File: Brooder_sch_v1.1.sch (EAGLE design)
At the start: 28 parts, among them J1 DCJ0202, U1 328P

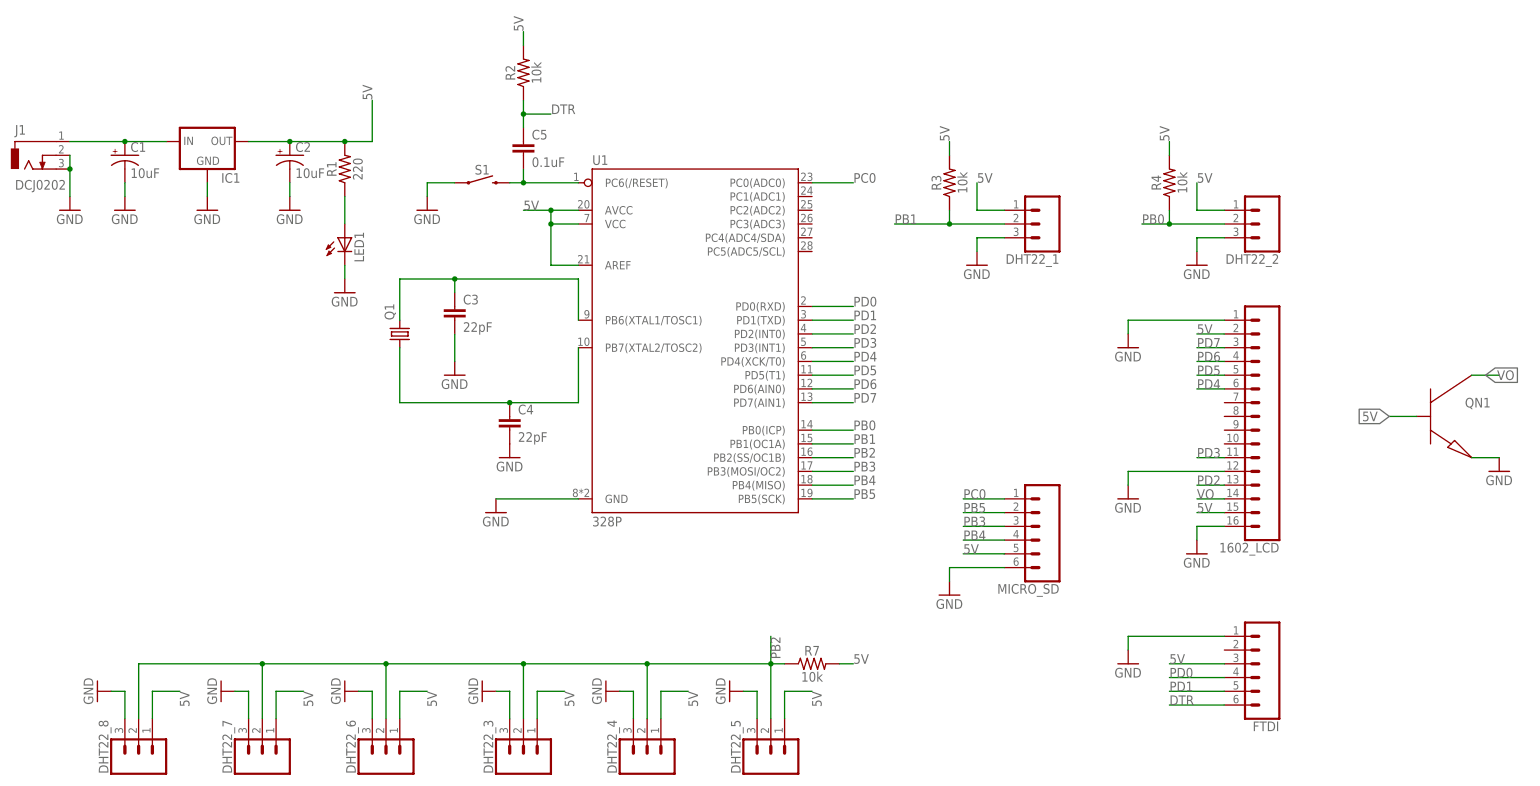
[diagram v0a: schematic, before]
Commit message: Adds the PCB layout
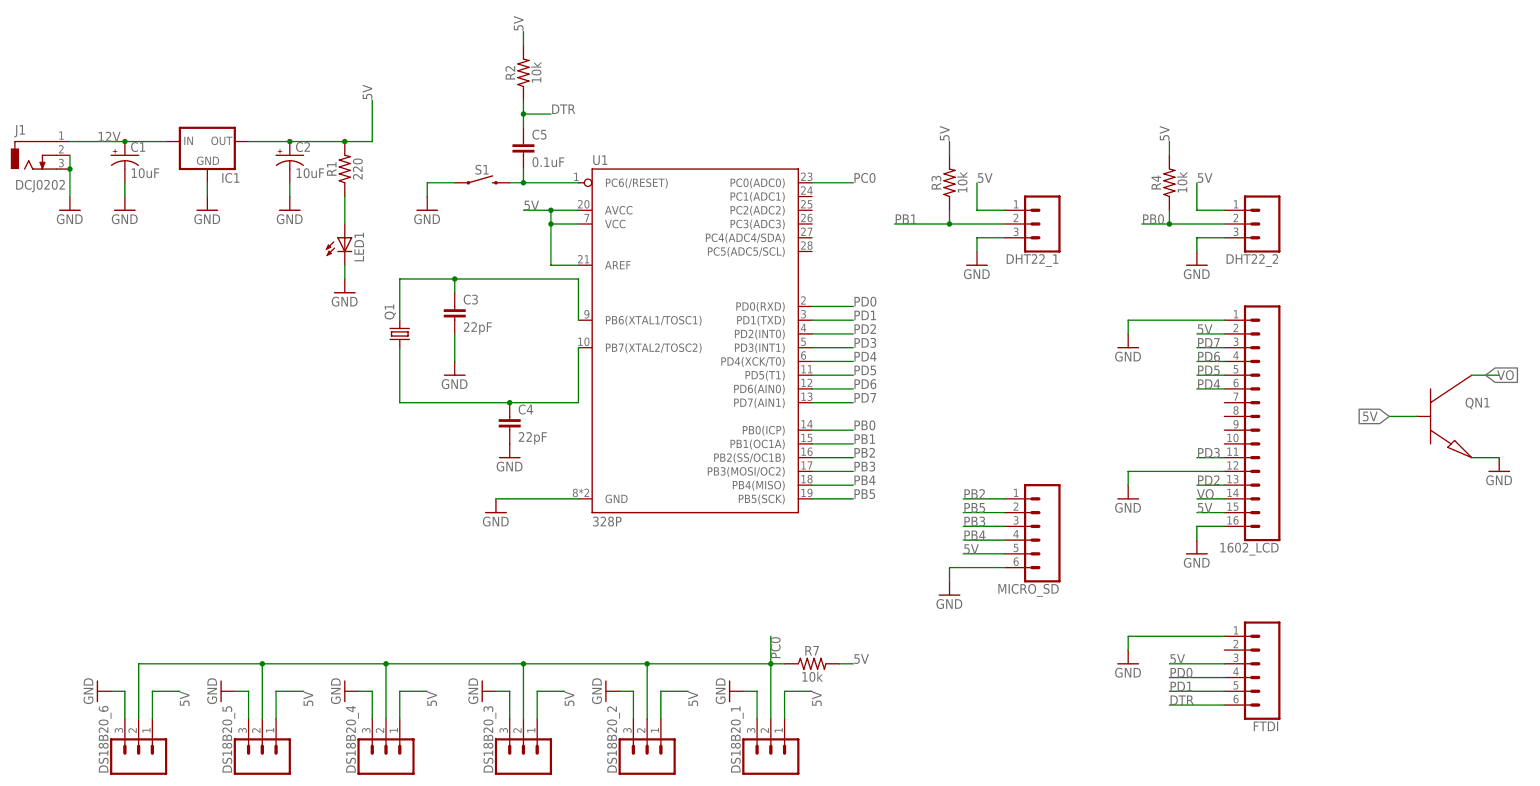
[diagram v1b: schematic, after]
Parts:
- renumbered DHT22_3 to DS18B20_3, DHT22_4 to DS18B20_2, DHT22_5 to DS18B20_1, DHT22_6 to DS18B20_4, DHT22_7 to DS18B20_5, DHT22_8 to DS18B20_6
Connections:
- net N$1 renamed 12V
- net PB2: now also MICRO_SD.1; no longer DS18B20_1.2, DS18B20_2.2, DS18B20_3.2, DS18B20_4.2, DS18B20_5.2, DS18B20_6.2, R7.1
- net PC0: now also DS18B20_1.2, DS18B20_2.2, DS18B20_3.2, DS18B20_4.2, DS18B20_5.2, DS18B20_6.2, R7.1; no longer MICRO_SD.1

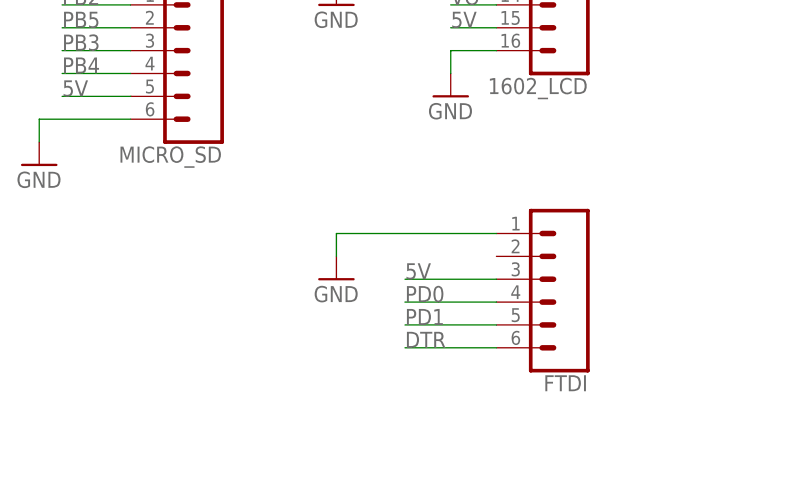
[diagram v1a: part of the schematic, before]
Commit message: Changes the lcd positioning, moves the microSD and corrects the FTDI pin mapping
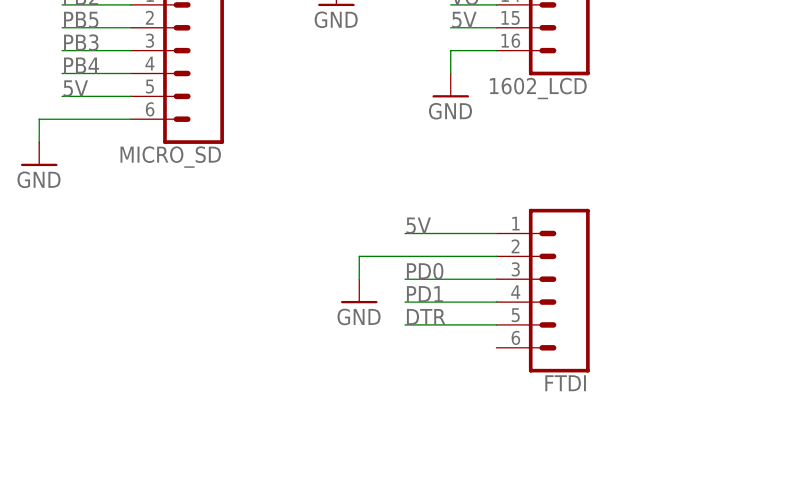
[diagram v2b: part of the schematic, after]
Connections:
- net 5V: now also FTDI.1; no longer FTDI.3
- net DTR: now also FTDI.5; no longer FTDI.6
- net GND: now also FTDI.2; no longer FTDI.1
- net PD0: now also FTDI.3; no longer FTDI.4
- net PD1: now also FTDI.4; no longer FTDI.5
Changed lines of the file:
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@@
 <part name="GND17" library="supply1" library_urn="urn:adsk.eagle:library:371" deviceset="GND" device=""/>
 <part name="FTDI" library="SparkFun-Connectors" deviceset="CONN_06" device="NO_SILK_FEMALE_PTH"/>
-<part name="GND18" library="supply1" library_urn="urn:adsk.eagle:library:371" deviceset="GND" device=""/>
 <part name="C5" library="SparkFun-Capacitors" deviceset="22PF" device="-PTH-2.54MM-200V-5%" value="0.1uF"/>
 <part name="DS18B20_3" library="SparkFun-Connectors" deviceset="CONN_03" device="" value="455-1750-1-ND"/>
@@
 <part name="DS18B20_6" library="SparkFun-Connectors" deviceset="CONN_03" device="" value="455-1750-1-ND"/>
 <part name="GND23" library="supply1" library_urn="urn:adsk.eagle:library:371" deviceset="GND" device=""/>
+<part name="GND18" library="supply1" library_urn="urn:adsk.eagle:library:371" deviceset="GND" device=""/>
 </parts>
 <sheets>
@@
 <attribute name="NAME" x="162.56" y="4.572" size="1.778" layer="95" font="vector" rot="R180"/>
 </instance>
-<instance part="GND18" gate="1" x="134.62" y="15.24" smashed="yes">
-<attribute name="VALUE" x="132.08" y="12.7" size="1.778" layer="96"/>
-</instance>
 <instance part="C5" gate="G$1" x="22.86" y="109.22" smashed="yes">
 <attribute name="NAME" x="24.384" y="112.141" size="1.778" layer="95" font="vector"/>
@@
 <instance part="GND23" gate="1" x="-55.88" y="10.16" smashed="yes" rot="R270">
 <attribute name="VALUE" x="-58.42" y="12.7" size="1.778" layer="96" rot="R270"/>
+</instance>
+<instance part="GND18" gate="1" x="137.16" y="12.7" smashed="yes">
+<attribute name="VALUE" x="134.62" y="10.16" size="1.778" layer="96"/>
 </instance>
 </instances>
@@
 </segment>
 <segment>
-<pinref part="FTDI" gate="G$1" pin="1"/>
-<wire x1="152.4" y1="20.32" x2="134.62" y2="20.32" width="0.1524" layer="91"/>
-<wire x1="134.62" y1="20.32" x2="134.62" y2="17.78" width="0.1524" layer="91"/>
-<pinref part="GND18" gate="1" pin="GND"/>
-</segment>
-<segment>
 <pinref part="DS18B20_3" gate="J$1" pin="3"/>
 <wire x1="20.32" y1="5.08" x2="20.32" y2="10.16" width="0.1524" layer="91"/>
@@
 <wire x1="-50.8" y1="10.16" x2="-53.34" y2="10.16" width="0.1524" layer="91"/>
 <pinref part="GND23" gate="1" pin="GND"/>
+</segment>
+<segment>
+<pinref part="FTDI" gate="G$1" pin="2"/>
+<wire x1="152.4" y1="17.78" x2="137.16" y2="17.78" width="0.1524" layer="91"/>
+<wire x1="137.16" y1="17.78" x2="137.16" y2="15.24" width="0.1524" layer="91"/>
+<pinref part="GND18" gate="1" pin="GND"/>
 </segment>
 </net>
@@
 </segment>
 <segment>
-<pinref part="FTDI" gate="G$1" pin="3"/>
-<wire x1="152.4" y1="15.24" x2="142.24" y2="15.24" width="0.1524" layer="91"/>
-<label x="142.24" y="15.24" size="1.778" layer="95"/>
-</segment>
-<segment>
 <pinref part="DS18B20_3" gate="J$1" pin="1"/>
 <wire x1="25.4" y1="5.08" x2="25.4" y2="10.16" width="0.1524" layer="91"/>
@@
 <wire x1="-45.72" y1="10.16" x2="-40.64" y2="10.16" width="0.1524" layer="91"/>
 <label x="-40.64" y="10.16" size="1.778" layer="95" rot="R270"/>
+</segment>
+<segment>
+<pinref part="FTDI" gate="G$1" pin="1"/>
+<wire x1="152.4" y1="20.32" x2="142.24" y2="20.32" width="0.1524" layer="91"/>
+<label x="142.24" y="20.32" size="1.778" layer="95"/>
 </segment>
 </net>
@@
 <net name="DTR" class="0">
 <segment>
-<pinref part="FTDI" gate="G$1" pin="6"/>
-<wire x1="152.4" y1="7.62" x2="142.24" y2="7.62" width="0.1524" layer="91"/>
-<label x="142.24" y="7.62" size="1.778" layer="95"/>
-</segment>
-<segment>
 <pinref part="C5" gate="G$1" pin="1"/>
 <pinref part="R2" gate="G$1" pin="1"/>
@@
 <label x="27.94" y="116.84" size="1.778" layer="95"/>
 </segment>
-</net>
-<net name="PD1" class="0">
 <segment>
 <pinref part="FTDI" gate="G$1" pin="5"/>
@@
 <label x="142.24" y="10.16" size="1.778" layer="95"/>
 </segment>
+</net>
+<net name="PD1" class="0">
 <segment>
 <pinref part="U1" gate="U1" pin="PD1(TXD)"/>
@@
 <label x="83.82" y="78.74" size="1.778" layer="95"/>
 </segment>
-</net>
-<net name="PD0" class="0">
 <segment>
 <pinref part="FTDI" gate="G$1" pin="4"/>
@@
 <label x="142.24" y="12.7" size="1.778" layer="95"/>
 </segment>
+</net>
+<net name="PD0" class="0">
 <segment>
 <pinref part="U1" gate="U1" pin="PD0(RXD)"/>
@@
 <label x="83.82" y="81.28" size="1.778" layer="95"/>
 </segment>
-</net>
+<segment>
+<pinref part="FTDI" gate="G$1" pin="3"/>
+<wire x1="152.4" y1="15.24" x2="142.24" y2="15.24" width="0.1524" layer="91"/>
+<label x="142.24" y="15.24" size="1.778" layer="95"/>
+</segment>
+</net>

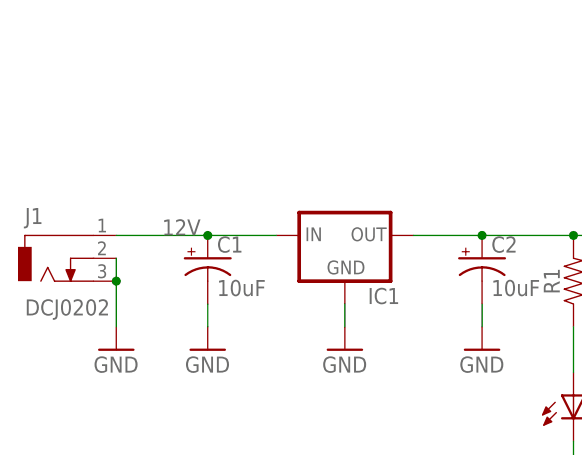
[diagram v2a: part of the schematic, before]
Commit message: Adds space for the rocker switch
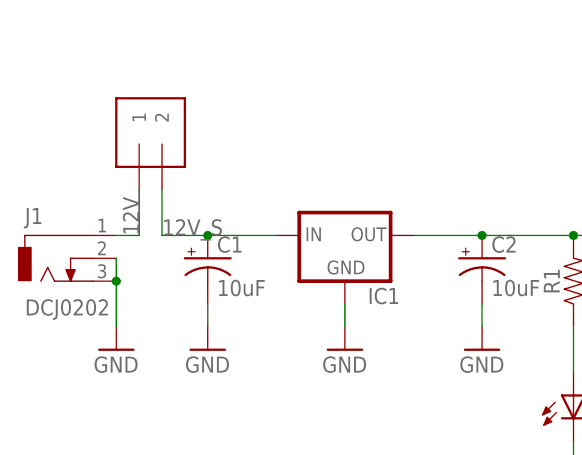
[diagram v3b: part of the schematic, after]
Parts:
- added J2: 1X2-3.5MM, adafruit:1X2-3.5MM
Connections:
- new net 12V_S: C1.+, IC1.IN, J2.2
- net 12V: now also J2.1; no longer C1.+, IC1.IN
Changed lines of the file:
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@@
 <part name="GND23" library="supply1" library_urn="urn:adsk.eagle:library:371" deviceset="GND" device=""/>
 <part name="GND18" library="supply1" library_urn="urn:adsk.eagle:library:371" deviceset="GND" device=""/>
+<part name="J2" library="adafruit" deviceset="1X2" device="-3.5MM"/>
 </parts>
 <sheets>
@@
 <attribute name="VALUE" x="134.62" y="10.16" size="1.778" layer="96"/>
 </instance>
+<instance part="J2" gate="G$1" x="-55.88" y="121.92" rot="R90"/>
 </instances>
 <busses>
@@
 <segment>
 <pinref part="J1" gate="G$1" pin="1"/>
-<pinref part="C1" gate="G$1" pin="+"/>
-<wire x1="-60.96" y1="111.76" x2="-50.8" y2="111.76" width="0.1524" layer="91"/>
-<pinref part="IC1" gate="1" pin="IN"/>
-<wire x1="-50.8" y1="111.76" x2="-43.18" y2="111.76" width="0.1524" layer="91"/>
-<junction x="-50.8" y="111.76"/>
-<label x="-55.88" y="111.76" size="1.778" layer="95"/>
+<wire x1="-60.96" y1="111.76" x2="-58.42" y2="111.76" width="0.1524" layer="91"/>
+<pinref part="J2" gate="G$1" pin="1"/>
+<wire x1="-58.42" y1="111.76" x2="-58.42" y2="116.84" width="0.1524" layer="91"/>
+<label x="-58.42" y="111.76" size="1.778" layer="95" rot="R90"/>
 </segment>
 </net>
@@
 </segment>
 </net>
+<net name="12V_S" class="0">
+<segment>
+<pinref part="C1" gate="G$1" pin="+"/>
+<pinref part="IC1" gate="1" pin="IN"/>
+<wire x1="-50.8" y1="111.76" x2="-43.18" y2="111.76" width="0.1524" layer="91"/>
+<pinref part="J2" gate="G$1" pin="2"/>
+<wire x1="-55.88" y1="116.84" x2="-55.88" y2="111.76" width="0.1524" layer="91"/>
+<wire x1="-55.88" y1="111.76" x2="-50.8" y2="111.76" width="0.1524" layer="91"/>
+<junction x="-50.8" y="111.76"/>
+<label x="-55.88" y="111.76" size="1.778" layer="95"/>
+</segment>
+</net>

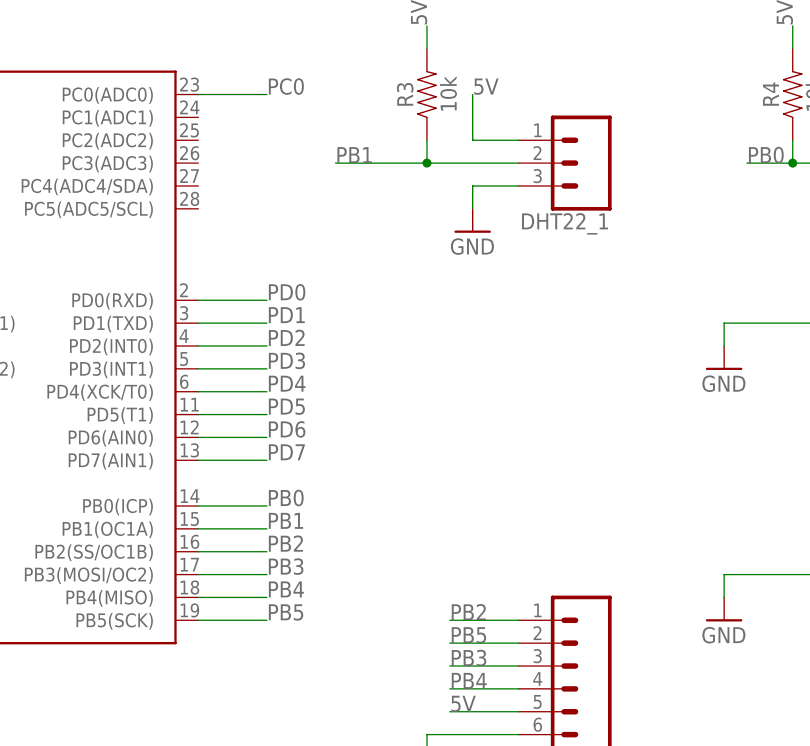
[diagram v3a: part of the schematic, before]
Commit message: Adds the RTC clock
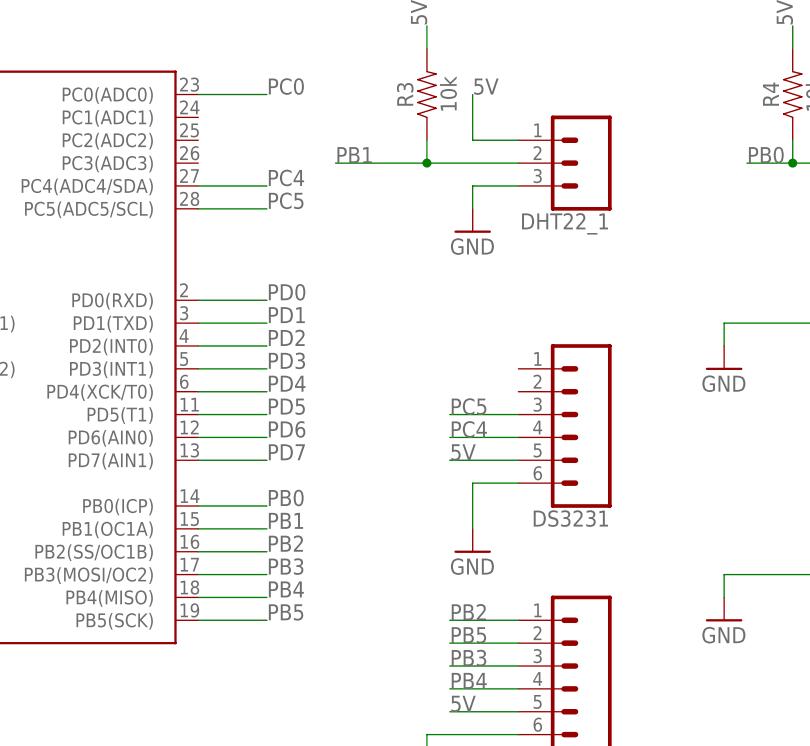
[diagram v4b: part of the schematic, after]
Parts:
- added DS3231: (no value), SparkFun-Connectors:CONN_06NO_SILK_FEMALE_PTH
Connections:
- new net PC4: DS3231.4, U1.PC4(ADC4/SDA)
- new net PC5: DS3231.3, U1.PC5(ADC5/SCL)
- net 5V: now also DS3231.5
- net GND: now also DS3231.6
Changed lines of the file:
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@@
 <part name="GND18" library="supply1" library_urn="urn:adsk.eagle:library:371" deviceset="GND" device=""/>
 <part name="J2" library="adafruit" deviceset="1X2" device="-3.5MM"/>
+<part name="DS3231" library="SparkFun-Connectors" deviceset="CONN_06" device="NO_SILK_FEMALE_PTH"/>
+<part name="GND24" library="supply1" library_urn="urn:adsk.eagle:library:371" deviceset="GND" device=""/>
 </parts>
 <sheets>
@@
 </instance>
 <instance part="J2" gate="G$1" x="-55.88" y="121.92" rot="R90"/>
+<instance part="DS3231" gate="G$1" x="116.84" y="68.58" smashed="yes" rot="R180">
+<attribute name="VALUE" x="121.92" y="78.486" size="1.778" layer="96" font="vector" rot="R180"/>
+<attribute name="NAME" x="121.92" y="57.912" size="1.778" layer="95" font="vector" rot="R180"/>
+</instance>
+<instance part="GND24" gate="1" x="106.68" y="53.34" smashed="yes">
+<attribute name="VALUE" x="104.14" y="50.8" size="1.778" layer="96"/>
+</instance>
 </instances>
 <busses>
@@
 <wire x1="137.16" y1="17.78" x2="137.16" y2="15.24" width="0.1524" layer="91"/>
 <pinref part="GND18" gate="1" pin="GND"/>
+</segment>
+<segment>
+<pinref part="DS3231" gate="G$1" pin="6"/>
+<wire x1="111.76" y1="60.96" x2="106.68" y2="60.96" width="0.1524" layer="91"/>
+<wire x1="106.68" y1="60.96" x2="106.68" y2="55.88" width="0.1524" layer="91"/>
+<pinref part="GND24" gate="1" pin="GND"/>
 </segment>
 </net>
@@
 <wire x1="152.4" y1="20.32" x2="142.24" y2="20.32" width="0.1524" layer="91"/>
 <label x="142.24" y="20.32" size="1.778" layer="95"/>
+</segment>
+<segment>
+<pinref part="DS3231" gate="G$1" pin="5"/>
+<wire x1="111.76" y1="63.5" x2="104.14" y2="63.5" width="0.1524" layer="91"/>
+<label x="104.14" y="63.5" size="1.778" layer="95"/>
 </segment>
 </net>
@@
 </segment>
 </net>
+<net name="PC4" class="0">
+<segment>
+<pinref part="DS3231" gate="G$1" pin="4"/>
+<wire x1="111.76" y1="66.04" x2="104.14" y2="66.04" width="0.1524" layer="91"/>
+<label x="104.14" y="66.04" size="1.778" layer="95"/>
+</segment>
+<segment>
+<pinref part="U1" gate="U1" pin="PC4(ADC4/SDA)"/>
+<wire x1="76.2" y1="93.98" x2="83.82" y2="93.98" width="0.1524" layer="91"/>
+<label x="83.82" y="93.98" size="1.778" layer="95"/>
+</segment>
+</net>
+<net name="PC5" class="0">
+<segment>
+<pinref part="DS3231" gate="G$1" pin="3"/>
+<wire x1="111.76" y1="68.58" x2="104.14" y2="68.58" width="0.1524" layer="91"/>
+<label x="104.14" y="68.58" size="1.778" layer="95"/>
+</segment>
+<segment>
+<pinref part="U1" gate="U1" pin="PC5(ADC5/SCL)"/>
+<wire x1="76.2" y1="91.44" x2="83.82" y2="91.44" width="0.1524" layer="91"/>
+<label x="83.82" y="91.44" size="1.778" layer="95"/>
+</segment>
+</net>
